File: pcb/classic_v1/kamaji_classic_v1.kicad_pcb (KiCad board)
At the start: 2 copper layers, 100 x 100 mm, 31 parts, among them J1 USB_A, J2 USB_B, J4 ISP, J5 P1, J6 P2, J7 P3, J8 P4, J9 P5, Q1 BS170, SW1 SW_Push, SW2 SW_Push, SW3 SW_Push, U1 ATmega328P-P

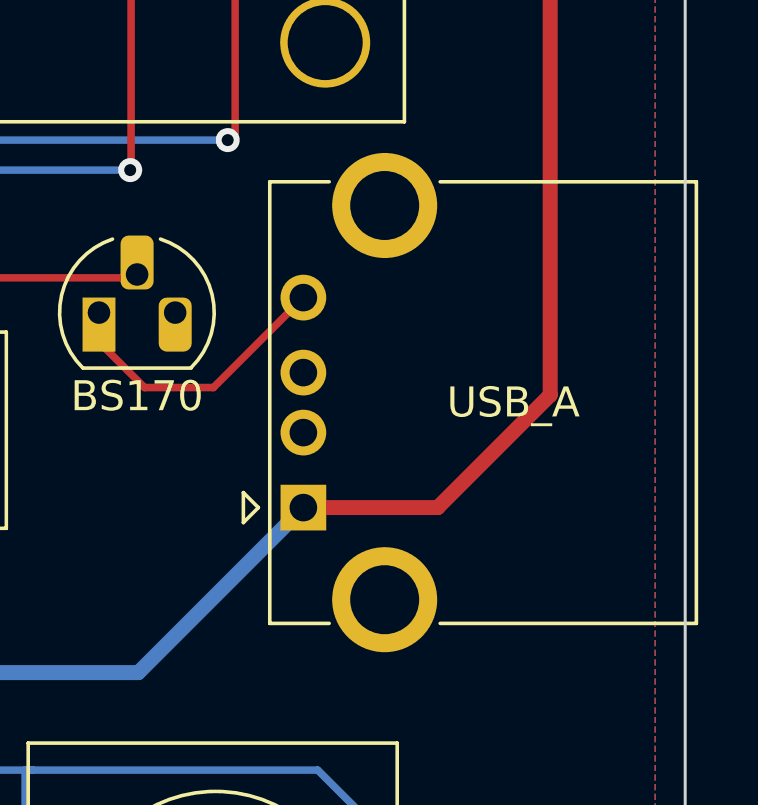
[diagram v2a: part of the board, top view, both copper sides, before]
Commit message: Update Classic V1 PCB
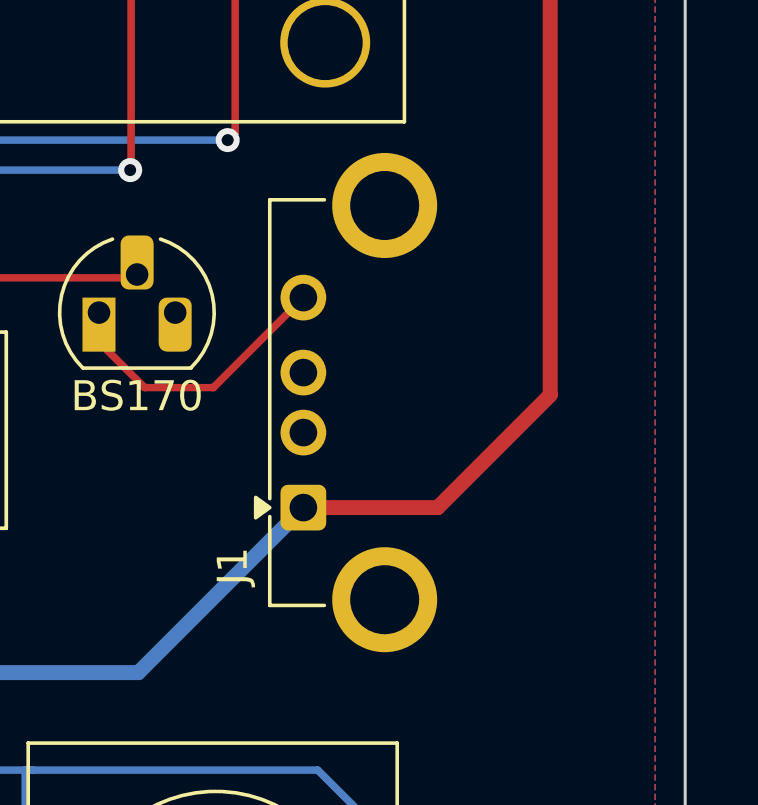
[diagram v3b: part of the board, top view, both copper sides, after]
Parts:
- J1: footprint Connector_USB:USB_A_CONNFLY_DS1095-WNR0 -> Connector_USB:USB_A_Connfly_DS1095
